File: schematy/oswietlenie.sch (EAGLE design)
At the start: 9 parts, among them U1 V_REG_317SINK

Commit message: update`
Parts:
- removed R1: 220R, rcl:R-EU_0204/5
- removed R2: 330R, rcl:R-EU_0204/5
- removed U1: V_REG_317SINK, SparkFun-IC-Power:V_REG_317SINK
- added D1, D2, D3: 1N4004, diode:1N4004
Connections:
- new net N$1: D1.C, D2.A
- net GND: no longer R2.1
- net N$5: now also D3.C; no longer R1.2, U1.OUT
- net N$6: now also D2.C, D3.A; no longer R1.1, R2.2, U1.ADJ
- net VCC: now also D1.A; no longer U1.IN
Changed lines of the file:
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@@
 <part name="GND5" library="supply1" library_urn="urn:adsk.eagle:library:371" deviceset="GND" device=""/>
 <part name="P+5" library="supply1" library_urn="urn:adsk.eagle:library:371" deviceset="+5V" device=""/>
-<part name="R1" library="rcl" library_urn="urn:adsk.eagle:library:334" deviceset="R-EU_" device="0204/5" package3d_urn="urn:adsk.eagle:package:23488/1" value="220R"/>
-<part name="R2" library="rcl" library_urn="urn:adsk.eagle:library:334" deviceset="R-EU_" device="0204/5" package3d_urn="urn:adsk.eagle:package:23488/1" value="330R"/>
-<part name="GND2" library="supply1" library_urn="urn:adsk.eagle:library:371" deviceset="GND" device=""/>
 <part name="~220V" library="jumper" library_urn="urn:adsk.eagle:library:252" deviceset="JP1E" device="" package3d_urn="urn:adsk.eagle:package:15455/1"/>
-<part name="U1" library="SparkFun-IC-Power" deviceset="V_REG_317" device="SINK"/>
+<part name="D1" library="diode" library_urn="urn:adsk.eagle:library:210" deviceset="1N4004" device="" package3d_urn="urn:adsk.eagle:package:43336/1"/>
+<part name="D2" library="diode" library_urn="urn:adsk.eagle:library:210" deviceset="1N4004" device="" package3d_urn="urn:adsk.eagle:package:43336/1"/>
+<part name="D3" library="diode" library_urn="urn:adsk.eagle:library:210" deviceset="1N4004" device="" package3d_urn="urn:adsk.eagle:package:43336/1"/>
 </parts>
 <sheets>
@@
 <instance part="E1" gate="G$1" x="19.05" y="78.74"/>
 <instance part="GND3" gate="1" x="3.81" y="22.86"/>
-<instance part="P+3" gate="VCC" x="-27.94" y="58.166"/>
+<instance part="P+3" gate="VCC" x="-38.1" y="45.466"/>
 <instance part="C1" gate="G$1" x="3.81" y="38.1"/>
 <instance part="U$2" gate="G$1" x="154.94" y="43.18"/>
@@
 <instance part="GND5" gate="1" x="132.08" y="66.04"/>
 <instance part="P+5" gate="1" x="142.24" y="76.2"/>
-<instance part="R1" gate="G$1" x="-5.08" y="45.72" rot="R90"/>
-<instance part="R2" gate="G$1" x="-5.08" y="33.02" rot="R90"/>
-<instance part="GND2" gate="1" x="-5.08" y="22.86"/>
 <instance part="~220V" gate="A" x="185.42" y="27.94" rot="R180"/>
-<instance part="U1" gate="G$1" x="-17.78" y="53.34"/>
+<instance part="D1" gate="1" x="-33.02" y="40.64"/>
+<instance part="D2" gate="1" x="-20.32" y="40.64"/>
+<instance part="D3" gate="1" x="-7.62" y="40.64"/>
 </instances>
 <busses>
@@
 <segment>
 <pinref part="P+3" gate="VCC" pin="VCC"/>
-<wire x1="-27.94" y1="55.626" x2="-27.94" y2="53.34" width="0.1524" layer="91"/>
-<pinref part="U1" gate="G$1" pin="IN"/>
-<wire x1="-27.94" y1="53.34" x2="-25.4" y2="53.34" width="0.1524" layer="91"/>
+<wire x1="-38.1" y1="42.926" x2="-38.1" y2="40.64" width="0.1524" layer="91"/>
+<pinref part="D1" gate="1" pin="A"/>
+<wire x1="-38.1" y1="40.64" x2="-35.56" y2="40.64" width="0.1524" layer="91"/>
 </segment>
 </net>
@@
 <wire x1="139.7" y1="68.58" x2="132.08" y2="68.58" width="0.1524" layer="91"/>
 <pinref part="JP1" gate="A" pin="2"/>
-</segment>
-<segment>
-<pinref part="R2" gate="G$1" pin="1"/>
-<pinref part="GND2" gate="1" pin="GND"/>
-<wire x1="-5.08" y1="27.94" x2="-5.08" y2="25.4" width="0.1524" layer="91"/>
 </segment>
 </net>
@@
 <net name="N$5" class="0">
 <segment>
-<pinref part="U1" gate="G$1" pin="OUT"/>
 <pinref part="C1" gate="G$1" pin="1"/>
 <pinref part="E1" gate="G$1" pin="+3.3V"/>
 <wire x1="13.97" y1="40.64" x2="3.81" y2="40.64" width="0.1524" layer="91"/>
+<pinref part="D3" gate="1" pin="C"/>
+<wire x1="-5.08" y1="40.64" x2="3.81" y2="40.64" width="0.1524" layer="91"/>
 <junction x="3.81" y="40.64"/>
-<wire x1="3.81" y1="53.34" x2="3.81" y2="40.64" width="0.1524" layer="91"/>
-<wire x1="-10.16" y1="53.34" x2="-5.08" y2="53.34" width="0.1524" layer="91"/>
-<pinref part="R1" gate="G$1" pin="2"/>
-<wire x1="-5.08" y1="53.34" x2="3.81" y2="53.34" width="0.1524" layer="91"/>
-<wire x1="-5.08" y1="50.8" x2="-5.08" y2="53.34" width="0.1524" layer="91"/>
-<junction x="-5.08" y="53.34"/>
+</segment>
+</net>
+<net name="N$1" class="0">
+<segment>
+<pinref part="D1" gate="1" pin="C"/>
+<pinref part="D2" gate="1" pin="A"/>
+<wire x1="-30.48" y1="40.64" x2="-22.86" y2="40.64" width="0.1524" layer="91"/>
 </segment>
 </net>
 <net name="N$6" class="0">
 <segment>
-<pinref part="R2" gate="G$1" pin="2"/>
-<wire x1="-5.08" y1="39.878" x2="-5.08" y2="38.1" width="0.1524" layer="91"/>
-<pinref part="R1" gate="G$1" pin="1"/>
-<wire x1="-5.08" y1="40.64" x2="-5.08" y2="38.1" width="0.1524" layer="91"/>
-<pinref part="U1" gate="G$1" pin="ADJ"/>
-<wire x1="-17.78" y1="45.72" x2="-17.78" y2="40.64" width="0.1524" layer="91"/>
-<wire x1="-17.78" y1="40.64" x2="-5.08" y2="40.64" width="0.1524" layer="91"/>
-<junction x="-5.08" y="40.64"/>
+<pinref part="D2" gate="1" pin="C"/>
+<pinref part="D3" gate="1" pin="A"/>
+<wire x1="-17.78" y1="40.64" x2="-10.16" y2="40.64" width="0.1524" layer="91"/>
 </segment>
 </net>

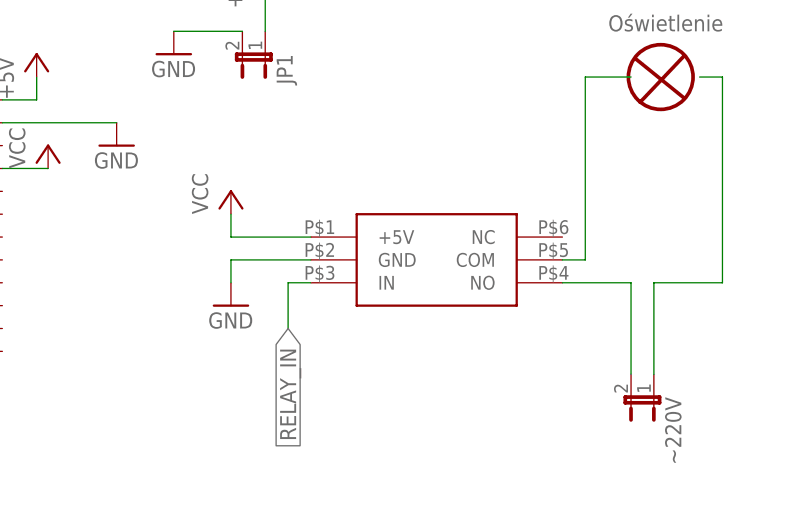
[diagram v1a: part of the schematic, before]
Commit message: poprawki po sprawdzeniu przez dr Swirniaka
pozostalo tylko sprawdzic pod katem ASAP i te male uwagi
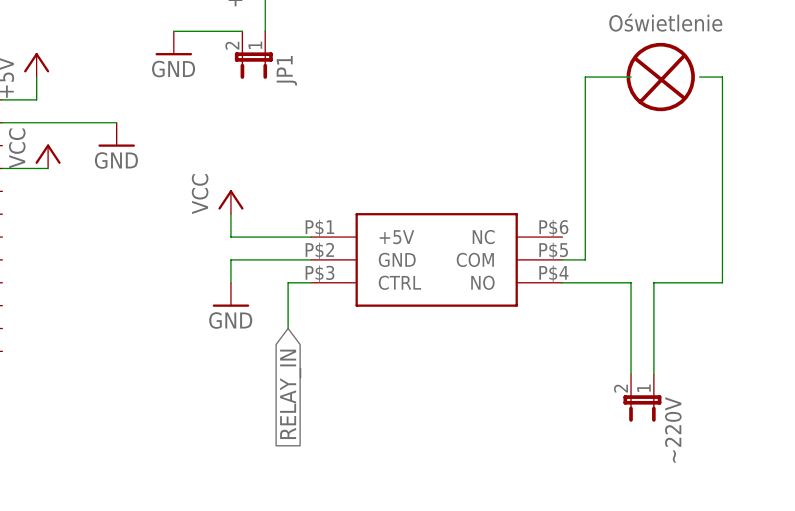
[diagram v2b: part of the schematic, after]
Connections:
- net RELAY_IN: now also U$2.CTRL; no longer U$2.IN
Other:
- note added: "Moduł Przekaźnika"
- note removed: "Przekaźnik"
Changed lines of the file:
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@@
 <wire x1="188.722" y1="65.786" x2="183.896" y2="60.706" width="0.4064" layer="94"/>
 <text x="180.34" y="68.58" size="1.778" layer="95">Oświetlenie</text>
-<text x="149.86" y="53.34" size="3.81" layer="111">Przekaźnik</text>
+<text x="147.32" y="50.8" size="3.81" layer="111">    Moduł
+Przekaźnika</text>
 </plain>
 <instances>
@@
 </segment>
 <segment>
-<pinref part="U$2" gate="G$1" pin="IN"/>
+<pinref part="U$2" gate="G$1" pin="CTRL"/>
 <wire x1="147.32" y1="40.64" x2="144.78" y2="40.64" width="0.1524" layer="91"/>
 <wire x1="144.78" y1="40.64" x2="144.78" y2="35.56" width="0.1524" layer="91"/>
